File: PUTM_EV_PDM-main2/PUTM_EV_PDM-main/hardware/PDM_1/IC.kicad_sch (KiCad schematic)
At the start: 19 parts, among them IC2 BTS722204ESAXUMA1

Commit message: lepsze footprinty
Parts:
- C29, C30, C31, C32, C33, C34, C35, C36: footprint (none) -> Capacitor_SMD:C_0603_1608Metric_Pad1.08x0.95mm_HandSolder
- D8: footprint (none) -> Diode_SMD:D_SMA
- R11, R12, R13, R14, R15, R16, R17, R18, R19: footprint (none) -> Resistor_SMD:R_0603_1608Metric_Pad0.98x0.95mm_HandSolder
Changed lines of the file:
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@@
       (effects (font (size 1.27 1.27)) (justify left))
     )
-    (property "Footprint" "" (at 128.27 64.77 0)
+    (property "Footprint" "Capacitor_SMD:C_0603_1608Metric_Pad1.08x0.95mm_HandSolder" (at 128.27 64.77 0)
       (effects (font (size 1.27 1.27)) hide)
     )
@@
       (effects (font (size 1.27 1.27)) (justify left))
     )
-    (property "Footprint" "" (at 119.38 113.03 0)
+    (property "Footprint" "Resistor_SMD:R_0603_1608Metric_Pad0.98x0.95mm_HandSolder" (at 119.38 113.03 0)
       (effects (font (size 1.27 1.27)) hide)
     )
@@
       (effects (font (size 1.27 1.27)))
     )
-    (property "Footprint" "" (at 119.38 91.44 0)
+    (property "Footprint" "Resistor_SMD:R_0603_1608Metric_Pad0.98x0.95mm_HandSolder" (at 119.38 91.44 0)
       (effects (font (size 1.27 1.27)) hide)
     )
@@
       (effects (font (size 1.27 1.27)) (justify left))
     )
-    (property "Footprint" "" (at 95.25 113.03 90)
-      (effects (font (size 1.27 1.27)) hide)
-    )
-    (property "Datasheet" "~" (at 95.25 113.03 90)
+    (property "Footprint" "Diode_SMD:D_SMA" (at 95.25 113.03 90)
+      (effects (font (size 1.27 1.27)) hide)
+    )
+    (property "Datasheet" "https://www.mouser.pl/ProductDetail/Taiwan-Semiconductor/SS34ALH?qs=A6eO%252BMLsxmQip%2FrgNup6RA%3D%3D" (at 95.25 113.03 90)
       (effects (font (size 1.27 1.27)) hide)
     )
@@
       (effects (font (size 1.27 1.27)))
     )
-    (property "Footprint" "" (at 104.14 71.12 0)
+    (property "Footprint" "Resistor_SMD:R_0603_1608Metric_Pad0.98x0.95mm_HandSolder" (at 104.14 71.12 0)
       (effects (font (size 1.27 1.27)) hide)
     )
@@
       (effects (font (size 1.27 1.27)) (justify left))
     )
-    (property "Footprint" "" (at 186.69 102.87 0)
+    (property "Footprint" "Capacitor_SMD:C_0603_1608Metric_Pad1.08x0.95mm_HandSolder" (at 186.69 102.87 0)
       (effects (font (size 1.27 1.27)) hide)
     )
@@
       (effects (font (size 1.27 1.27)))
     )
-    (property "Footprint" "" (at 119.38 93.98 0)
+    (property "Footprint" "Resistor_SMD:R_0603_1608Metric_Pad0.98x0.95mm_HandSolder" (at 119.38 93.98 0)
       (effects (font (size 1.27 1.27)) hide)
     )
@@
       (effects (font (size 1.27 1.27)) (justify left))
     )
-    (property "Footprint" "" (at 182.88 93.98 0)
+    (property "Footprint" "Capacitor_SMD:C_0603_1608Metric_Pad1.08x0.95mm_HandSolder" (at 182.88 93.98 0)
       (effects (font (size 1.27 1.27)) hide)
     )
@@
       (effects (font (size 1.27 1.27)))
     )
-    (property "Footprint" "" (at 104.14 106.68 0)
+    (property "Footprint" "Resistor_SMD:R_0603_1608Metric_Pad0.98x0.95mm_HandSolder" (at 104.14 106.68 0)
       (effects (font (size 1.27 1.27)) hide)
     )
@@
       (effects (font (size 1.27 1.27)))
     )
-    (property "Footprint" "" (at 86.36 106.68 0)
+    (property "Footprint" "Resistor_SMD:R_0603_1608Metric_Pad0.98x0.95mm_HandSolder" (at 86.36 106.68 0)
       (effects (font (size 1.27 1.27)) hide)
     )
@@
       (effects (font (size 1.27 1.27)))
     )
-    (property "Footprint" "" (at 119.38 88.9 0)
+    (property "Footprint" "Resistor_SMD:R_0603_1608Metric_Pad0.98x0.95mm_HandSolder" (at 119.38 88.9 0)
       (effects (font (size 1.27 1.27)) hide)
     )
@@
       (effects (font (size 1.27 1.27)) (justify left))
     )
-    (property "Footprint" "" (at 177.8 85.09 0)
+    (property "Footprint" "Capacitor_SMD:C_0603_1608Metric_Pad1.08x0.95mm_HandSolder" (at 177.8 85.09 0)
       (effects (font (size 1.27 1.27)) hide)
     )
@@
       (effects (font (size 1.27 1.27)) (justify left))
     )
-    (property "Footprint" "" (at 173.99 76.2 0)
+    (property "Footprint" "Capacitor_SMD:C_0603_1608Metric_Pad1.08x0.95mm_HandSolder" (at 173.99 76.2 0)
       (effects (font (size 1.27 1.27)) hide)
     )
@@
       (effects (font (size 1.27 1.27)))
     )
-    (property "Footprint" "" (at 119.38 96.52 0)
+    (property "Footprint" "Resistor_SMD:R_0603_1608Metric_Pad0.98x0.95mm_HandSolder" (at 119.38 96.52 0)
       (effects (font (size 1.27 1.27)) hide)
     )
@@
       (effects (font (size 1.27 1.27)) (justify right))
     )
-    (property "Footprint" "" (at 128.27 53.34 0)
+    (property "Footprint" "Capacitor_SMD:C_0603_1608Metric_Pad1.08x0.95mm_HandSolder" (at 128.27 53.34 0)
       (effects (font (size 1.27 1.27)) hide)
     )
@@
       (effects (font (size 1.27 1.27)) (justify left))
     )
-    (property "Footprint" "" (at 77.47 113.03 0)
+    (property "Footprint" "Capacitor_SMD:C_0603_1608Metric_Pad1.08x0.95mm_HandSolder" (at 77.47 113.03 0)
       (effects (font (size 1.27 1.27)) hide)
     )
@@
       (effects (font (size 1.27 1.27)) (justify right))
     )
-    (property "Footprint" "" (at 115.57 53.34 0)
+    (property "Footprint" "Capacitor_SMD:C_0603_1608Metric_Pad1.08x0.95mm_HandSolder" (at 115.57 53.34 0)
       (effects (font (size 1.27 1.27)) hide)
     )
@@
       (effects (font (size 1.27 1.27)))
     )
-    (property "Footprint" "" (at 121.92 59.69 0)
-      (effects (font (size 1.27 1.27)) hide)
-    )
+    (property "Footprint" "Resistor_SMD:R_0603_1608Metric_Pad0.98x0.95mm_HandSolder" (at 121.92 59.69 0)
+      (effects (font (size 1.27 1.27)) hide)
+    )

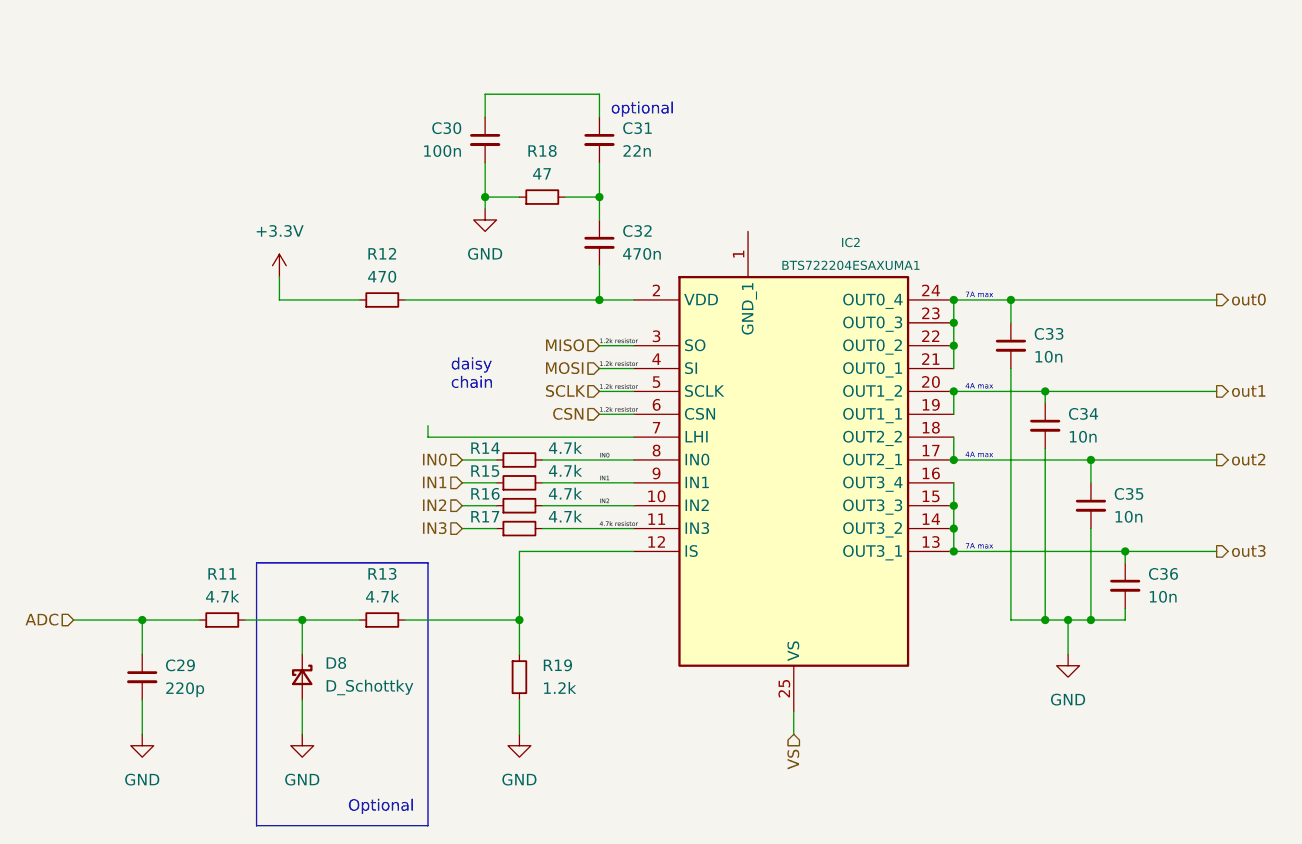
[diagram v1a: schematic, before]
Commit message: nowe połączenia
dodane połączenia z STM
dodane złącza
dodane LED
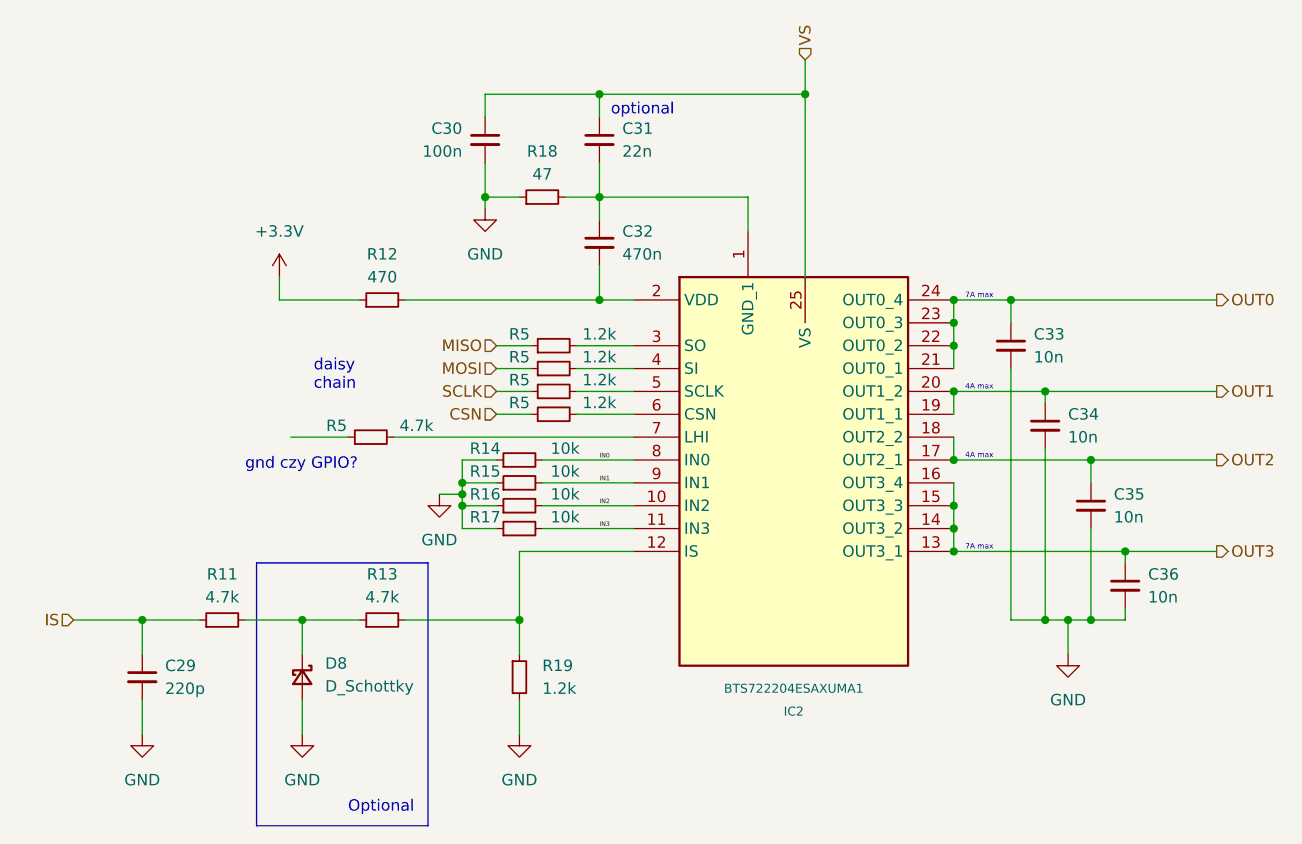
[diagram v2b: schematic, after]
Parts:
- added R5 (x4): 1.2k, Resistor_SMD:R_0603_1608Metric, symbol Device:R_Small
- added R5: 4.7k, Resistor_SMD:R_0603_1608Metric, symbol Device:R_Small
- R14, R15, R16, R17: value 4.7k -> 10k
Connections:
- net 4.7k resistor is gone; now on net IN3: IC2.11 (IN3), R17.2
- net CSN: now also R5.1; no longer IC2.3 (SO), IC2.4 (SI), IC2.5 (SCLK), IC2.6 (CSN)
- net GND: now also R14.1, R15.1, R16.1, R17.1
- net IN0: no longer R14.1
- net IN1: no longer R15.1
- net IN2: no longer R16.1
- net IN3: no longer R17.1
- net VS: now also C30.1, C31.1
- net at C31.2, C32.1, R18.2: now also IC2.1 (GND_1)
- net at IC2.7 (LHI): now also R5.2
- net ADC renamed IS
- net out0 renamed OUT0
- net out1 renamed OUT1
- net out2 renamed OUT2
- net out3 renamed OUT3
- new net: IC2.5 (SCLK), R5.2
- new net: IC2.3 (SO), R5.2
- new net: IC2.6 (CSN), R5.2
- new net: IC2.4 (SI), R5.2
- new net MISO: R5.1
- new net MOSI: R5.1
- new net SCLK: R5.1
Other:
- note added: "gnd czy GPIO?"
- moved on the sheet: IC2

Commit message: małe zmiany
dodano złącza
zmieniono parę footprintów
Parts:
- renumbered R5 to R2, R5 to R3, R5 to R4, R5 to R58
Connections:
- net LHI: now reaches R58.1
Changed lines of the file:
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@@
     (effects (font (size 1.27 1.27)) (justify left))
+  )
+  (hierarchical_label "LHI" (shape input) (at 93.98 86.36 180) (fields_autoplaced)
+    (effects (font (size 1.27 1.27)) (justify right))
   )
   (hierarchical_label "VS" (shape input) (at 151.13 44.45 90) (fields_autoplaced)
@@
   (symbol (lib_id "Device:R_Small") (at 123.19 81.28 90) (unit 1)
     (in_bom yes) (on_board yes) (dnp no)
-    (property "Reference" "R5" (at 119.38 80.01 90)
+    (property "Reference" "R4" (at 119.38 80.01 90)
       (effects (font (size 1.27 1.27)))
     )
@@
   (symbol (lib_id "Device:R_Small") (at 123.19 76.2 90) (unit 1)
     (in_bom yes) (on_board yes) (dnp no)
-    (property "Reference" "R5" (at 119.38 74.93 90)
+    (property "Reference" "R2" (at 119.38 74.93 90)
       (effects (font (size 1.27 1.27)))
     )
@@
   (symbol (lib_id "Device:R_Small") (at 102.87 86.36 90) (unit 1)
     (in_bom yes) (on_board yes) (dnp no)
-    (property "Reference" "R5" (at 99.06 85.09 90)
+    (property "Reference" "R58" (at 99.06 85.09 90)
       (effects (font (size 1.27 1.27)))
     )
@@
   (symbol (lib_id "Device:R_Small") (at 123.19 78.74 90) (unit 1)
     (in_bom yes) (on_board yes) (dnp no)
-    (property "Reference" "R5" (at 119.38 77.47 90)
-      (effects (font (size 1.27 1.27)))
-    )
+    (property "Reference" "R3" (at 119.38 77.47 90)
+      (effects (font (size 1.27 1.27)))
+    )

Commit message: Koniec połączeń sygnałów
Wszystkie sygnały z stm poprowadzone
Zmienione ułożenie połączeń do złącz
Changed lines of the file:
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@@
     (effects (font (size 1.27 1.27)) (justify right))
   )
-  (hierarchical_label "MISO" (shape input) (at 116.84 76.2 180) (fields_autoplaced)
+  (hierarchical_label "MISO" (shape output) (at 116.84 76.2 180) (fields_autoplaced)
     (effects (font (size 1.27 1.27)) (justify right))
   )
